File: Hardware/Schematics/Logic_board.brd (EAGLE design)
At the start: 99 x 48.5 mm, 64 parts, among them IC3 74AC373DW, J1 1X2-3.5MM, J2 1X2-3.5MM, J4 1X2-3.5MM, Q1 BSL207SP, Q2 BSL207SP, Q3 MOSFET-NCHANNELSMD, Q8 4.096MHz, U1 ESP-32S

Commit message: Created new logicboard with isolation from HV side.
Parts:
- removed BUTTON1, BUTTON2, BUTTON3: (no value), pinhead:1X03
- removed C10, C9: 100nF, rcl:C1206
- removed C11, C12, C14, C15: 220nF, rcl:C1206
- removed C13, C16: 22nF, rcl:C1206
- removed D4: (no value), diode:DO-214AC
- removed IC3: 74AC373DW, 74xx-eu:SO20W
- removed J2, J4: 1X2-3.5MM, adafruit:1X2-3.5MM
- removed JTAG, UART: -, pinhead:1X04
- removed Q1, Q2: BSL207SP, transistor-fet:SC74_INFINEON
- removed Q3: MOSFET-NCHANNELSMD, fets:SOT23-3
- removed Q7: (no value), adafruit:SOT23
- removed Q8: 4.096MHz, crystal:HC49U70
- removed R17: 10K, rcl:R0805
- removed U$12: POWER_SOCKET_EU, PowerSocket:POWER_SOCKET_EU
- removed U$2, U$3: RELAYPTH, SRD-05VDC-SL-C:SRD-05VDC-SL-C
- removed U$4: ADUM1410, PowerSocket:SOIC-16
- removed U$5: HLK-PM03, PowerSocket:HLK-PM03
- removed U$9: CS5463, PowerSocket:SO24L
- added B1, B2, B3: JST-XH-03-PIN-LONG-PAD, Rembrandt:JST-XH-03-PACKAGE-LONG-PAD
- added IC1: ADUM1250, analog-devices-3:SO8-COOL
- added JP2: (no value), pinhead:2X04
- C1, C17, C18, C2, C3, C4, C5, C6, C7: device rcl:C1206 -> rcl:C0805
- C8: value 100nF -> 100µF; device rcl:C1206 -> rcl:E3,5-8
- JP1: device pinhead:2X16/90 -> pinhead:2X09/90
- R10: value 1K -> 10K
- R3: device resistor:R0805 -> rcl:R0805
- R4: value 1M -> 10K
- R5: value 560 -> 1K; device rcl:R1206 -> rcl:R0805
- R8: value 12m -> 1K; device rcl:R2512 -> rcl:R0805
- U$1: value STEP_DOWN -> PCF8574AT; device PowerSocket:STEP_DOWN -> i2c:SO16
- moved JP1 560.8 mm to (56.6, 12.2), turned to 270 degrees
- moved R10 543.6 mm to (8.90, 40.9), flipped to the bottom, turned to 180 degrees
- moved R9 539.3 mm to (47.2, 8.40)
- moved R8 499.3 mm to (48.3, 5.00), turned to 90 degrees
- moved R6 471.3 mm to (36.4, 4.80), turned to 270 degrees
- moved R5 452.4 mm to (38.6, 7.50), turned to 270 degrees
- moved R4 438.4 mm to (8.90, 28.7), flipped to the bottom, turned to 180 degrees
- moved C6 432.3 mm to (48.4, 22.5), turned to 90 degrees
- moved C8 431.6 mm to (8.80, 19.0), turned to 270 degrees
- moved J1 424.3 mm to (50.9, 39.9)
- moved C7 419.0 mm to (35.0, 12.9), flipped to the bottom, turned to 270 degrees
- moved C5 410.8 mm to (35.5, 7.90)
- moved U$8 396.9 mm to (45.0, 40.9), turned to 180 degrees
- moved R3 335.4 mm to (8.80, 34.9), flipped to the bottom, turned to 180 degrees
- moved U$1 327.9 mm to (20.9, 38.8), flipped to the bottom, turned to 90 degrees
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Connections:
- removed net 1.8V: Q1.4, U$1.P$3
- removed net N$1: J1.2, U$8.AC1
- removed net N$10: Q1.3, Q3.3, R3.1
- removed net N$12: D4.A, Q7.3, U$2.COIL0, U$3.COIL0
- removed net N$13: J1.1, U$8.AC2
- removed net N$14: U$6.7, U$6.8
- removed net N$17: Q8.1, U$9.1
- removed net N$2: JTAG.1, U1.23
- removed net N$24: U$6.6
- removed net N$26: R10.1, R5.2, R6.1, R8.1, U$2.SWCOMMON
- removed net N$27: U$6.5
- removed net N$28: U$6.4
- removed net N$29: U$6.14
- removed net N$3: JTAG.2, U1.16
- removed net N$30: C15.2, C16.2, R9.2, U$9.15
- removed net N$31: U$6.13
- removed net N$32: IC3.11, R17.1, U1.9
- removed net N$33: IC3.3, U1.12
- removed net N$34: IC3.4, U1.11
- removed net N$35: IC3.7, U1.10
- removed net N$36: U$6.12
- removed net N$37: U$6.11
- removed net N$38: C8.1, U$9.11, U$9.12
- removed net N$39: U$6.10
- removed net N$4: JTAG.3, U1.14
- removed net N$40: U$4.6
- removed net N$41: U$4.5
- removed net N$42: C14.1, C16.1, R10.2, U$9.16
- removed net N$45: U$4.4
- removed net N$49: U$4.3
- removed net N$5: JTAG.4, U1.13
- removed net N$50: Q8.2, U$9.24
- removed net N$51: U$7.3
- removed net N$52: U$7.4
- removed net N$53: U$7.5
- removed net N$54: U$11.6, U$7.6
- removed net N$55: U$11.5
- removed net N$6: J4.2, U$5.AC1
- removed net N$70: U1.35, UART.2
- removed net N$77: U1.34, UART.3
- removed net N$8: J4.1, U$5.AC2
- removed net NULL1: J2.1, R4.1, U$3.SWCOMMON
- removed net NULL1_OUT: U$12.AC1, U$3.SWCLOSED
- removed net PHASE1: J2.2, R8.2, R9.1
- removed net PHASE1_OUT: U$12.AC2, U$2.SWCLOSED
- removed net RELAY1: U$4.13
- removed net RELAY2: U$4.12
- removed net RELAY3: U$4.11
- removed net RELAY_SUPL_CTRL: Q2.3, Q3.1, U$4.14
- removed net RELAY_SUPPLY: D4.C, Q1.1, Q1.2, Q1.5, Q1.6, Q2.1, Q2.2, Q2.5, Q2.6, U$2.COIL1, U$3.COIL1
- removed net RESET: U$11.12, U$9.19
- removed net VIN+1: C12.2, C13.2, R4.2, R5.1, U$9.9
- removed net VIN-1: C11.1, C13.1, R6.2, U$9.10
- new net AC1: J1.1, U$8.AC1
- new net AC2: J1.2, U$8.AC2
- new net CS1_HV: JP1.7, U$7.13
- new net CS2_HV: JP1.6, U$7.14
- new net CS3_HV: JP1.3, U$11.11
- new net PC8574_INT: U$6.11, U1.37
- new net PC8574_INT_HV: JP1.15, U$6.6
- new net RX: JP2.4, U1.34
- new net SCL: IC1.3, R6.2, U$1.14, U1.33
- new net SCL2: IC1.6, JP1.13, R8.2
- new net SCLK_HV: JP1.8, U$7.12
- new net SDA: IC1.2, R5.2, U$1.15, U1.31
- new net SDA2: IC1.7, JP1.12, R9.2
- new net SDI_HV: JP1.9, U$7.11
- new net SDO_HV: JP1.16, U$6.5
- new net TCK: JP2.5, U1.16
- new net TDI: JP2.1, U1.14
- new net TDO: JP2.7, U1.23
- new net TMS: JP2.3, U1.13
- new net TX: JP2.6, U1.35
- net +5V: now also C1.2, IC1.8, JP1.1, JP1.11, JP1.18, JP1.4, R8.1, R9.1; no longer C10.1, C5.1, C9.1, Q2.4, R3.2, U$1.P$2, U$4.16, U$5.+VO, U$9.14, U$9.3
- net BUTTON1: now also B1.3, R4.2, U$1.4; no longer BUTTON1.3, U1.33
- net BUTTON2: now also B2.3, R3.2, U$1.5; no longer BUTTON2.3, U1.30
- net BUTTON3: now also B3.3, R10.2, U$1.6; no longer BUTTON3.3, U1.28
- net CS1: now also U$7.4, U1.28; no longer U$7.13, U$9.7
- net CS2: now also U$7.3, U1.26; no longer U$7.14
- net CS3: now also U$11.6, U1.27; no longer U$11.11
- net GND: now also C5.1, C8.-, IC1.4, JP2.8, R10.1, R3.1, R4.1, U$1.2, U$1.3, U$1.8, U$11.3, U$11.4, U$11.5; no longer C1.2, IC3.1, IC3.10, IC3.13, IC3.14, IC3.17, IC3.18, IC3.8, R17.2, U$4.2, U$4.7, U$4.8, UART.1
- net GND1: now also C1.1, IC1.5, JP1.10, JP1.14, JP1.17, JP1.2, JP1.5, U$6.3, U$6.4, U$6.7, U$6.8; no longer C10.2, C11.2, C12.1, C14.2, C15.1, C5.2, C8.2, C9.2, Q3.2, Q7.2, U$1.P$1, U$1.P$4, U$4.15, U$4.9, U$5.-VO, U$9.13, U$9.4, U$9.8
- net LED1: now also U1.12; no longer U1.31
- net LED2: now also U1.11; no longer U1.29
- net LED3: now also U1.8; no longer U1.27
- net N$11: now also B3.2; no longer BUTTON3.2
- net N$7: now also B2.2; no longer BUTTON2.2
- net N$9: now also B1.2; no longer BUTTON1.2
- net SCLK: now also U$7.5, U1.29; no longer U$7.12, U$9.5
- net SDI: now also U$7.6, U1.30; no longer U$7.11, U$9.23
- net SDO: now also U$6.12, U1.36; no longer U$6.3, U$9.6
- net VCC: now also B1.1, B2.1, B3.1, C5.2, C8.+, IC1.1, JP2.2, R5.1, R6.1, U$1.1, U$1.16; no longer BUTTON1.1, BUTTON2.1, BUTTON3.1, C1.1, IC3.20, U$4.1, UART.4
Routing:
- net VCC: track 0.00 -> 148.5 mm, vias 0 -> 3
- net GND1: track 0.00 -> 70.0 mm
- net RX: track 0.00 -> 53.9 mm
- net TX: track 0.00 -> 53.4 mm
- net SCL: track 0.00 -> 49.8 mm, vias 0 -> 1
- net FLASH: track 0.00 -> 49.7 mm, vias 0 -> 1
- net +5V: track 0.00 -> 48.6 mm
- net SDA: track 0.00 -> 47.1 mm, vias 0 -> 1
- net TDO: track 0.00 -> 28.1 mm
- net TMS: track 0.00 -> 26.7 mm
- net TDI: track 0.00 -> 26.2 mm
- net TCK: track 0.00 -> 25.4 mm
- net LED3_SWITCHED: track 0.00 -> 23.4 mm
- net AC1: track 0.00 -> 22.8 mm
- net BUTTON1: track 0.00 -> 20.0 mm, vias 0 -> 1
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- added copper zone on layer 1, net +5V
- added copper zone on layer 1, net GND
- added copper zone on layer 16, net GND
- added copper zone on layer 16, net GND1
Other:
- board size 99 x 48.5 mm -> 54.5 x 48.5 mm

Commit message: Relay board placement mostly done. Routing ~50% done.
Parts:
- added C9: 100nF, rcl:C0805
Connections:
- net GND: now also C9.2
- net VCC: now also C9.1
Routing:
- net VCC: track 148.5 -> 151.1 mm
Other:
- board size 54.5 x 48.5 mm -> 54.5 x 48.7 mm
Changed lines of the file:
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@@
 <grid distance="0.1" unitdist="mm" unit="mm" style="lines" multiple="1" display="no" altdistance="1" altunitdist="mm" altunit="mm"/>
 <layers>
-<layer number="1" name="Top" color="4" fill="1" visible="yes" active="yes"/>
+<layer number="1" name="Top" color="4" fill="1" visible="no" active="yes"/>
 <layer number="2" name="Route2" color="1" fill="3" visible="no" active="yes"/>
 <layer number="3" name="Route3" color="4" fill="3" visible="no" active="yes"/>
@@
 <layer number="14" name="Route14" color="1" fill="6" visible="no" active="yes"/>
 <layer number="15" name="Route15" color="4" fill="6" visible="no" active="yes"/>
-<layer number="16" name="Bottom" color="1" fill="1" visible="no" active="yes"/>
+<layer number="16" name="Bottom" color="1" fill="1" visible="yes" active="yes"/>
 <layer number="17" name="Pads" color="2" fill="1" visible="yes" active="yes"/>
 <layer number="18" name="Vias" color="2" fill="1" visible="yes" active="yes"/>
 <layer number="19" name="Unrouted" color="6" fill="1" visible="yes" active="yes"/>
 <layer number="20" name="Dimension" color="15" fill="1" visible="yes" active="yes"/>
-<layer number="21" name="tPlace" color="7" fill="1" visible="yes" active="yes"/>
-<layer number="22" name="bPlace" color="7" fill="1" visible="no" active="yes"/>
-<layer number="23" name="tOrigins" color="15" fill="1" visible="yes" active="yes"/>
-<layer number="24" name="bOrigins" color="15" fill="1" visible="no" active="yes"/>
-<layer number="25" name="tNames" color="7" fill="1" visible="yes" active="yes"/>
-<layer number="26" name="bNames" color="7" fill="1" visible="no" active="yes"/>
-<layer number="27" name="tValues" color="7" fill="1" visible="yes" active="yes"/>
-<layer number="28" name="bValues" color="7" fill="1" visible="no" active="yes"/>
+<layer number="21" name="tPlace" color="7" fill="1" visible="no" active="yes"/>
+<layer number="22" name="bPlace" color="7" fill="1" visible="yes" active="yes"/>
+<layer number="23" name="tOrigins" color="15" fill="1" visible="no" active="yes"/>
+<layer number="24" name="bOrigins" color="15" fill="1" visible="yes" active="yes"/>
+<layer number="25" name="tNames" color="7" fill="1" visible="no" active="yes"/>
+<layer number="26" name="bNames" color="7" fill="1" visible="yes" active="yes"/>
+<layer number="27" name="tValues" color="7" fill="1" visible="no" active="yes"/>
+<layer number="28" name="bValues" color="7" fill="1" visible="yes" active="yes"/>
 <layer number="29" name="tStop" color="7" fill="3" visible="no" active="yes"/>
 <layer number="30" name="bStop" color="7" fill="6" visible="no" active="yes"/>
@@
 <layer number="37" name="tTest" color="7" fill="1" visible="no" active="yes"/>
 <layer number="38" name="bTest" color="7" fill="1" visible="no" active="yes"/>
-<layer number="39" name="tKeepout" color="4" fill="11" visible="yes" active="yes"/>
-<layer number="40" name="bKeepout" color="1" fill="11" visible="no" active="yes"/>
-<layer number="41" name="tRestrict" color="4" fill="10" visible="yes" active="yes"/>
-<layer number="42" name="bRestrict" color="1" fill="10" visible="no" active="yes"/>
+<layer number="39" name="tKeepout" color="4" fill="11" visible="no" active="yes"/>
+<layer number="40" name="bKeepout" color="1" fill="11" visible="yes" active="yes"/>
+<layer number="41" name="tRestrict" color="4" fill="10" visible="no" active="yes"/>
+<layer number="42" name="bRestrict" color="1" fill="10" visible="yes" active="yes"/>
 <layer number="43" name="vRestrict" color="2" fill="10" visible="no" active="yes"/>
 <layer number="44" name="Drills" color="7" fill="1" visible="yes" active="yes"/>
@@
 <layer number="49" name="Reference" color="7" fill="1" visible="no" active="yes"/>
 <layer number="50" name="dxf" color="7" fill="1" visible="no" active="no"/>
-<layer number="51" name="tDocu" color="7" fill="1" visible="yes" active="yes"/>
-<layer number="52" name="bDocu" color="7" fill="1" visible="no" active="yes"/>
+<layer number="51" name="tDocu" color="7" fill="1" visible="no" active="yes"/>
+<layer number="52" name="bDocu" color="7" fill="1" visible="yes" active="yes"/>
 <layer number="53" name="tGND_GNDA" color="7" fill="9" visible="no" active="no"/>
 <layer number="54" name="bGND_GNDA" color="1" fill="9" visible="no" active="no"/>
@@
 <board>
 <plain>
-<wire x1="54.7" y1="0.3" x2="54.7" y2="48.8" width="0.5" layer="20"/>
-<wire x1="54.7" y1="48.8" x2="0.2" y2="48.8" width="0.5" layer="20"/>
-<wire x1="0.2" y1="48.8" x2="0.2" y2="0.3" width="0.5" layer="20"/>
+<wire x1="54.7" y1="0.3" x2="54.7" y2="49" width="0.5" layer="20"/>
+<wire x1="54.7" y1="49" x2="0.2" y2="49" width="0.5" layer="20"/>
+<wire x1="0.2" y1="49" x2="0.2" y2="0.3" width="0.5" layer="20"/>
 <wire x1="54.7" y1="0.3" x2="45.2" y2="0.3" width="0.5" layer="20"/>
 <wire x1="45.2" y1="0.3" x2="44.7" y2="0.8" width="0.5" layer="20" curve="-90"/>
@@
 <element name="R4" library="rcl" package="R0805" value="10K" x="8.9" y="28.7" rot="MR180"/>
 <element name="R10" library="rcl" package="R0805" value="10K" x="8.9" y="40.9" rot="MR180"/>
+<element name="C9" library="rcl" library_urn="urn:adsk.eagle:library:334" package="C0805" value="100nF" x="15.4" y="34.1" rot="MR90"/>
 </elements>
 <signals>
@@
 <via x="1.7" y="16.7" extent="1-16" drill="0.4" diameter="1"/>
 <via x="32.1" y="2.7" extent="1-16" drill="0.4" diameter="1"/>
+<contactref element="C9" pad="2"/>
 </signal>
 <signal name="VCC">
@@
 <wire x1="4.86" y1="31.9" x2="4.86" y2="25.8" width="0.3048" layer="1"/>
 <wire x1="4.86" y1="31.9" x2="4.86" y2="38" width="0.3048" layer="1"/>
-<wire x1="17.8266" y1="34.355" x2="17.8266" y2="32.9266" width="0.2" layer="16"/>
+<wire x1="17.8266" y1="33.5" x2="17.8266" y2="34.355" width="0.2" layer="16"/>
+<wire x1="17.8266" y1="33.5" x2="17.8266" y2="32.9266" width="0.2" layer="16"/>
 <wire x1="17.8266" y1="32.9266" x2="15.6" y2="30.7" width="0.2" layer="16"/>
 <wire x1="23.9734" y1="34.355" x2="26.155" y2="34.355" width="0.2" layer="16"/>
@@
 <wire x1="12.03" y1="10.5" x2="9.4" y2="10.5" width="0.5" layer="16"/>
 <wire x1="11.3" y1="10.5" x2="9.4" y2="10.5" width="0.5" layer="1"/>
+<contactref element="C9" pad="1"/>
+<wire x1="15.4" y1="33.15" x2="17.4766" y2="33.15" width="0.254" layer="16"/>
+<wire x1="17.4766" y1="33.15" x2="17.8266" y2="33.5" width="0.254" layer="16"/>
 </signal>
 <signal name="TDO">

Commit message: Power board routing done. Still missing adjustments of soldermask and silkscreen on both powerboard and logic board.
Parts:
- R5, R6, R8, R9: value 1K -> 2.5K
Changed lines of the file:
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@@
 <element name="U$1" library="i2c" package="SO16" value="PCF8574AT" x="20.9" y="38.8" rot="MR90"/>
 <element name="JP1" library="pinhead" library_urn="urn:adsk.eagle:library:325" package="2X09/90" value="" x="56.6" y="12.2" rot="R270"/>
-<element name="R8" library="rcl" package="R0805" value="1K" x="48.3" y="5" rot="R90"/>
-<element name="R9" library="rcl" package="R0805" value="1K" x="47.2" y="8.4"/>
-<element name="R5" library="rcl" package="R0805" value="1K" x="38.6" y="7.5" rot="R270"/>
-<element name="R6" library="rcl" package="R0805" value="1K" x="36.4" y="4.8" rot="R270"/>
+<element name="R8" library="rcl" package="R0805" value="2.5K" x="48.3" y="5" rot="R90"/>
+<element name="R9" library="rcl" package="R0805" value="2.5K" x="47.2" y="8.4"/>
+<element name="R5" library="rcl" package="R0805" value="2.5K" x="38.6" y="7.5" rot="R270"/>
+<element name="R6" library="rcl" package="R0805" value="2.5K" x="36.4" y="4.8" rot="R270"/>
 <element name="B1" library="Rembrandt" package="JST-XH-03-PACKAGE-LONG-PAD" value="JST-XH-03-PIN-LONG-PAD" x="7.4" y="25.8"/>
 <element name="B2" library="Rembrandt" package="JST-XH-03-PACKAGE-LONG-PAD" value="JST-XH-03-PIN-LONG-PAD" x="7.4" y="31.9"/>

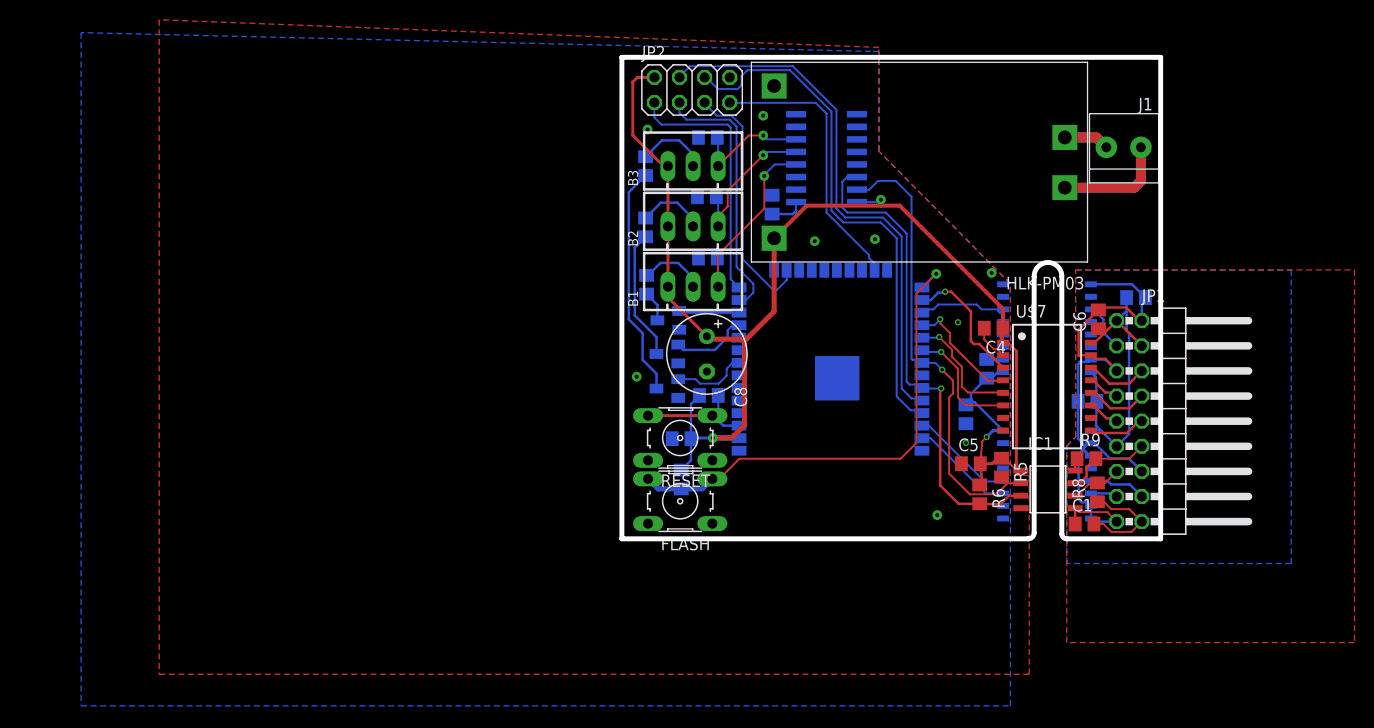
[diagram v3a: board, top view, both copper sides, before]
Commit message: Made Logic Board a bit smaller.
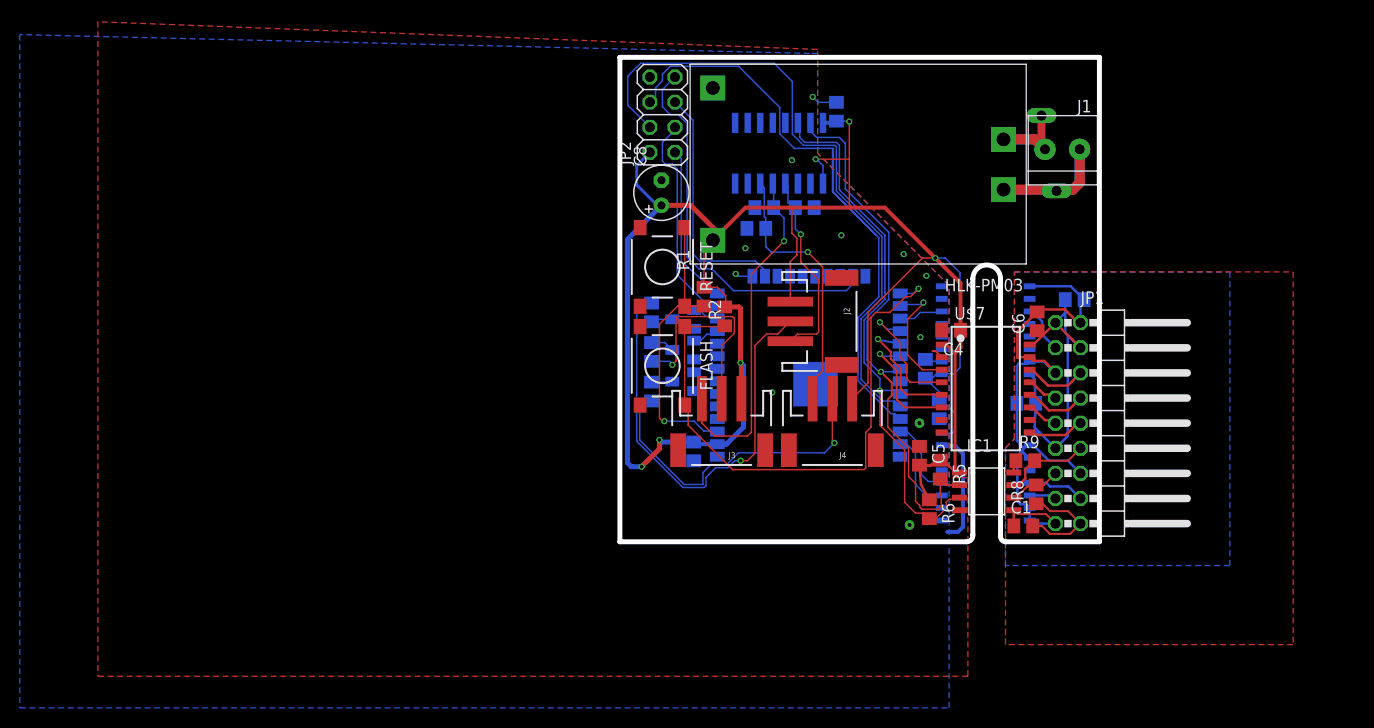
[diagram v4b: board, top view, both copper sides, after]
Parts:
- removed B1, B2, B3: JST-XH-03-PIN-LONG-PAD, Rembrandt:JST-XH-03-PACKAGE-LONG-PAD
- added J2, J3, J4: 3-PIN SMD, SparkFun-Connectors:JST-3-SMD
- added R11: S14K11, varistor:S14K11
- C8: device rcl:E3,5-8 -> rcl:E2,5-6
- FLASH, RESET: device switch-omron:B3F-10XX -> switch-tact:DTSM-6
- moved R22 22.8 mm to (3.20, 15.2), turned to 90 degrees
- moved RESET 17.4 mm to (4.30, 27.8), turned to 270 degrees
- moved R2 17.1 mm to (10.6, 22.8), flipped to the top
- moved C8 16.9 mm to (4.20, 35.3), turned to 90 degrees
- moved FLASH 13.8 mm to (4.30, 17.8), turned to 270 degrees
- moved R20 12.6 mm to (3.20, 19.2), turned to 90 degrees
- moved C9 11.4 mm to (21.9, 43.5)
- moved R4 11.0 mm to (18.7, 33.8), turned to 0 degrees
- moved R10 10.4 mm to (13.8, 31.7)
- moved R1 10.0 mm to (8.50, 24.8), flipped to the top, turned to 90 degrees
- moved C1 6.20 mm to (40.8, 1.60)
- moved C18 6.20 mm to (46.0, 24.5)
- moved JP1 6.20 mm to (50.4, 12.0)
- moved R5 6.20 mm to (32.4, 7.30)
- moved R9 6.20 mm to (41.0, 8.20)
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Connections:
- net AC1: now also R11.2
- net AC2: now also R11.1
- net BUTTON1: now also J2.3; no longer B1.3
- net BUTTON2: now also J3.3; no longer B2.3
- net BUTTON3: now also J4.3; no longer B3.3
- net FLASH: now also FLASH.1, FLASH.2; no longer FLASH.3, FLASH.4
- net GND: now also FLASH.3, FLASH.4, RESET.3, RESET.4; no longer FLASH.1, FLASH.2, RESET.1, RESET.2
- net N$11: now also J4.2; no longer B3.2
- net N$66: now also RESET.1, RESET.2; no longer RESET.3, RESET.4
- net N$7: now also J3.2; no longer B2.2
- net N$9: now also J2.2; no longer B1.2
- net VCC: now also J2.1, J3.1, J4.1; no longer B1.1, B2.1, B3.1
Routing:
- net VCC: track 151.1 -> 213.1 mm, vias 3 -> 6
- net N$9: track 6.74 -> 46.4 mm, vias 0 -> 1
- net N$11: track 7.26 -> 33.6 mm, vias 0 -> 1
- net LED3_SWITCHED: track 23.4 -> 2.12 mm
- net BUTTON2: track 15.6 -> 35.2 mm
- net N$66: track 11.9 -> 31.1 mm, vias 0 -> 1
- net TX: track 53.4 -> 68.7 mm
- net N$7: track 6.90 -> 21.9 mm, vias 0 -> 1
- net BUTTON3: track 12.3 -> 27.0 mm
- net GND: track 5.37 -> 19.2 mm, vias 9 -> 11
- net RX: track 53.9 -> 65.8 mm
- net TDO: track 28.1 -> 39.5 mm
- net LED2_SWITCHED: track 13.2 -> 2.41 mm
- net TDI: track 26.2 -> 16.2 mm
- net SDA: track 47.1 -> 56.5 mm
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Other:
- board size 54.5 x 48.7 mm -> 48.5 x 49 mm
